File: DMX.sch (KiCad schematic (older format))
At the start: 12 parts, among them SW1 SW_DIP_x09, U10 ST485CDR, U11 NPIC6C596

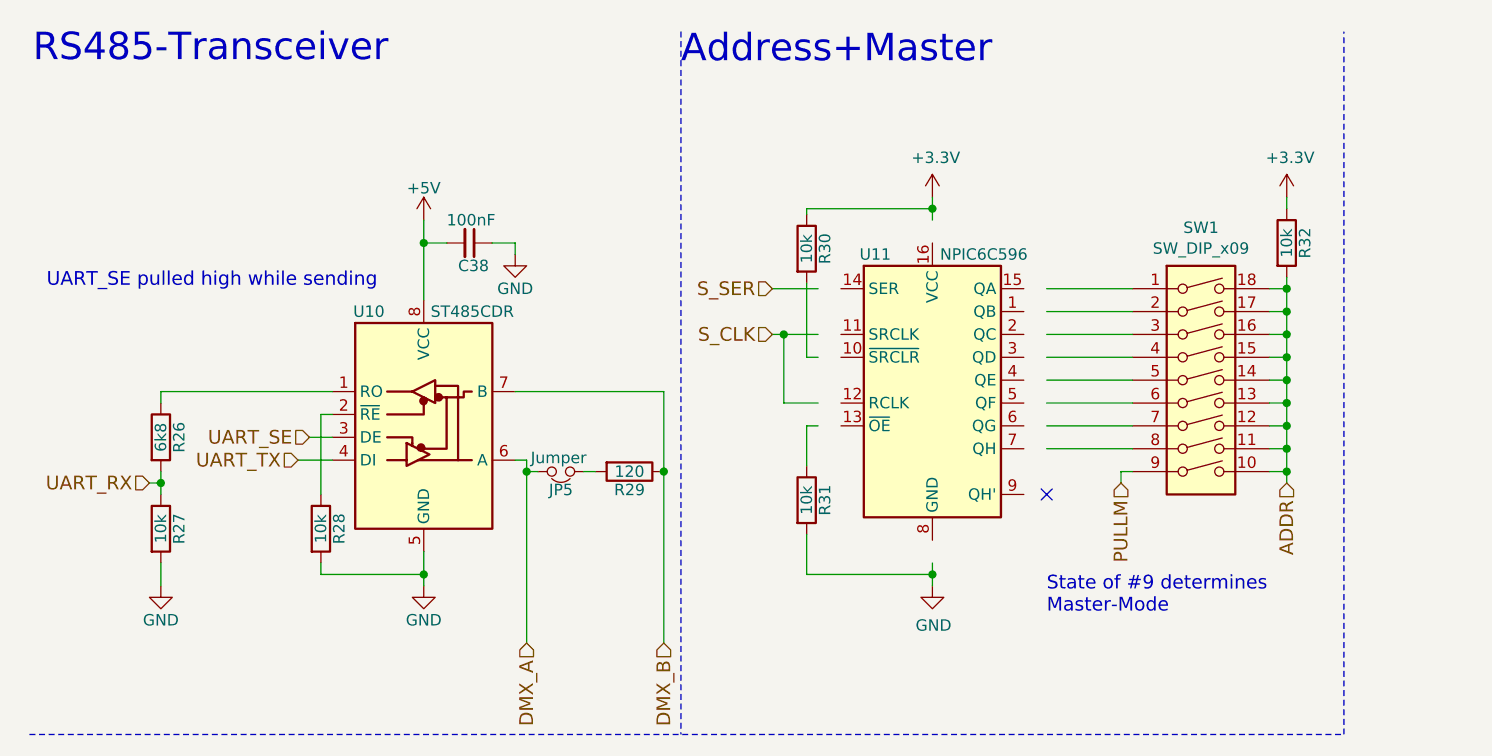
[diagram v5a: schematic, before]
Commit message: Migrated connectors to new libraries
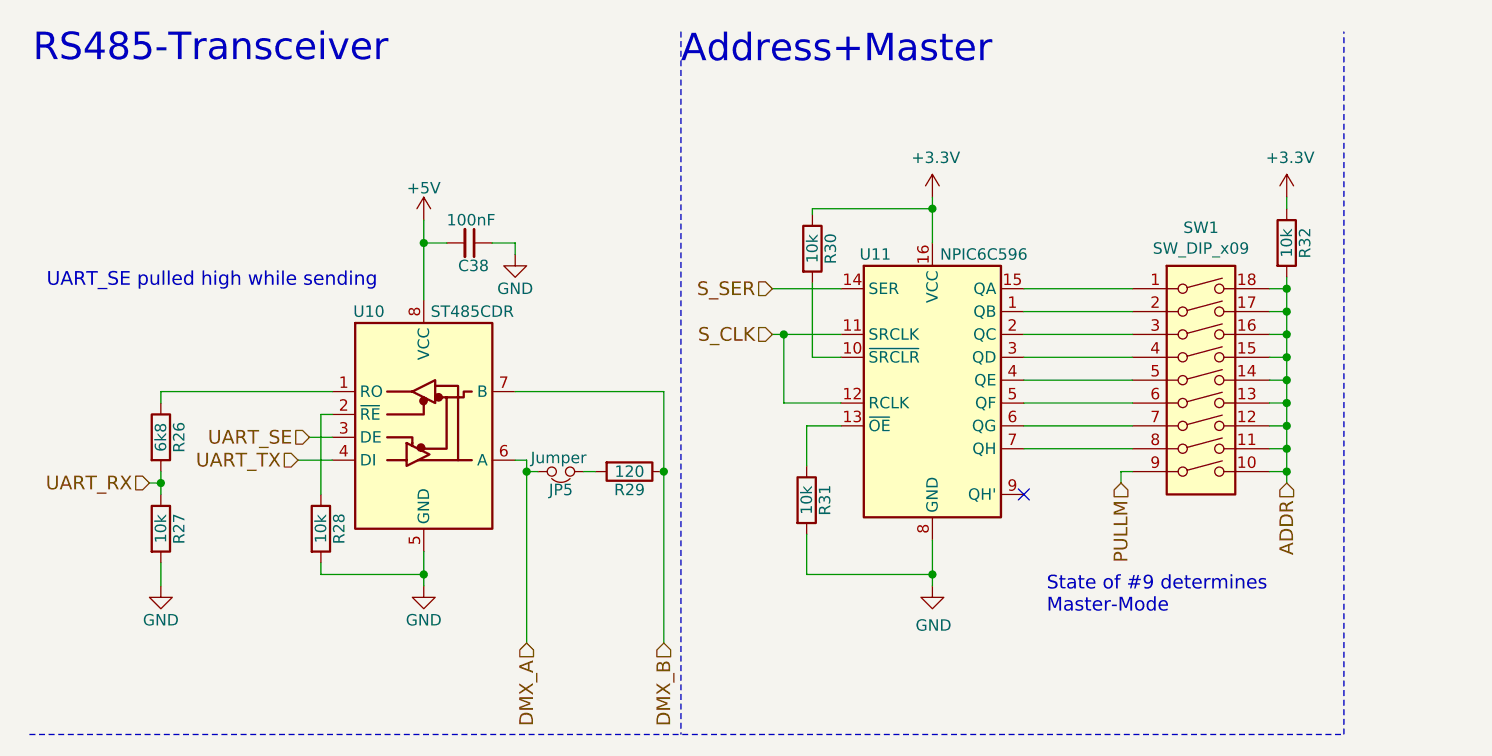
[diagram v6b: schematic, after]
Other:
- moved on the sheet: R30
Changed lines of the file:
@@
 $EndComp
 Wire Wire Line
-	4425 1250 4425 1300
+	4425 1250 4425 1400
 $Comp
 L power:GND #PWR096
@@
 $EndComp
 Wire Wire Line
-	4425 2850 4425 2800
-NoConn ~ 4925 2500
+	4425 2850 4425 2700
+NoConn ~ 4825 2500
 $Comp
 L Switch:SW_DIP_x09 SW1
@@
 $EndComp
 Wire Wire Line
-	4925 1600 5300 1600
+	4825 1600 5300 1600
 Wire Wire Line
-	4925 1800 5300 1800
+	4825 1800 5300 1800
 Wire Wire Line
-	5300 1900 4925 1900
+	5300 1900 4825 1900
 Wire Wire Line
-	4925 2000 5300 2000
+	4825 2000 5300 2000
 Wire Wire Line
-	5300 2100 4925 2100
+	5300 2100 4825 2100
 Wire Wire Line
-	4925 2200 5300 2200
+	4825 2200 5300 2200
 Wire Wire Line
-	4925 2300 5300 2300
+	4825 2300 5300 2300
 Wire Wire Line
-	4925 1700 5300 1700
+	4825 1700 5300 1700
 Wire Wire Line
 	5975 1550 5975 1600
@@
 	3875 2375 3875 2200
 Wire Wire Line
-	3875 2200 3925 2200
+	3875 2200 4025 2200
 $Comp
 L Device:R R30
 U 1 1 5B61520A
-P 3875 1425
-F 0 "R30" V 3955 1425 50  0000 C CNN
-F 1 "10k" V 3875 1425 50  0000 C CNN
-F 2 "Resistor_SMD:R_0603_1608Metric" V 3805 1425 50  0001 C CNN
-F 3 "" H 3875 1425 50  0001 C CNN
-F 4 "https://www.digikey.com/product-detail/en/bourns-inc/CR0603-FX-1002HLF/CR0603-FX-1002HLFCT-ND/3925297" V 3875 1425 50  0001 C CNN "Buy"
-	1    3875 1425
+P 3900 1425
+F 0 "R30" V 3980 1425 50  0000 C CNN
+F 1 "10k" V 3900 1425 50  0000 C CNN
+F 2 "Resistor_SMD:R_0603_1608Metric" V 3830 1425 50  0001 C CNN
+F 3 "" H 3900 1425 50  0001 C CNN
+F 4 "https://www.digikey.com/product-detail/en/bourns-inc/CR0603-FX-1002HLF/CR0603-FX-1002HLFCT-ND/3925297" V 3900 1425 50  0001 C CNN "Buy"
+	1    3900 1425
 	1    0    0    -1
 $EndComp
 Wire Wire Line
-	3875 1900 3875 1575
+	3900 1900 3900 1575
 Wire Wire Line
 	3875 2675 3875 2850
 Wire Wire Line
-	3875 1900 3925 1900
+	3900 1900 4025 1900
 Text HLabel 3725 1600 0    60   Input ~ 0
 S_SER
 Wire Wire Line
-	3725 1600 3925 1600
+	3725 1600 4025 1600
 Text HLabel 3725 1800 0    60   Input ~ 0
 S_CLK
@@
 	3775 1800 3775 2100
 Wire Wire Line
-	3775 2100 3925 2100
+	3775 2100 4025 2100
 Connection ~ 3775 1800
 Wire Wire Line
-	3775 1800 3925 1800
+	3775 1800 4025 1800
 Text HLabel 5250 2450 3    60   Input ~ 0
 PULLM
@@
 Connection ~ 4425 2850
 Wire Wire Line
-	3875 1275 3875 1250
+	3900 1275 3900 1250
 Wire Wire Line
-	3875 1250 4425 1250
+	3900 1250 4425 1250
 Connection ~ 4425 1250
 Wire Wire Line

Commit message: Replaced OOS 10k-Resistor
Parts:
- R27, R28, R30, R31, R32: Buy https://www.digikey.com/product-detail/en/bourns-inc/CR0603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 -> https://www.digikey.com/short/jw22d4
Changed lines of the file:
@@
 F 2 "Resistor_SMD:R_0603_1608Metric" V 980 2650 50  0001 C CNN
 F 3 "" H 1050 2650 50  0001 C CNN
-F 4 "https://www.digikey.com/product-detail/en/bourns-inc/CR0603-FX-1002HLF/CR0603-FX-1002HLFCT-ND/3925297" V 1050 2650 50  0001 C CNN "Buy"
+F 4 "https://www.digikey.com/short/jw22d4" V 1050 2650 50  0001 C CNN "Buy"
 	1    1050 2650
 	1    0    0    -1
@@
 F 2 "Resistor_SMD:R_0603_1608Metric" V 1680 2650 50  0001 C CNN
 F 3 "" H 1750 2650 50  0001 C CNN
-F 4 "https://www.digikey.com/product-detail/en/bourns-inc/CR0603-FX-1002HLF/CR0603-FX-1002HLFCT-ND/3925297" V 1750 2650 50  0001 C CNN "Buy"
+F 4 "https://www.digikey.com/short/jw22d4" V 1750 2650 50  0001 C CNN "Buy"
 	1    1750 2650
 	1    0    0    -1
@@
 F 2 "Resistor_SMD:R_0603_1608Metric" V 5905 1400 50  0001 C CNN
 F 3 "" H 5975 1400 50  0001 C CNN
-F 4 "https://www.digikey.com/product-detail/en/bourns-inc/CR0603-FX-1002HLF/CR0603-FX-1002HLFCT-ND/3925297" V 5975 1400 50  0001 C CNN "Buy"
+F 4 "https://www.digikey.com/short/jw22d4" V 5975 1400 50  0001 C CNN "Buy"
 	1    5975 1400
 	1    0    0    -1
@@
 F 2 "Resistor_SMD:R_0603_1608Metric" V 3805 2525 50  0001 C CNN
 F 3 "" H 3875 2525 50  0001 C CNN
-F 4 "https://www.digikey.com/product-detail/en/bourns-inc/CR0603-FX-1002HLF/CR0603-FX-1002HLFCT-ND/3925297" V 3875 2525 50  0001 C CNN "Buy"
+F 4 "https://www.digikey.com/short/jw22d4" V 3875 2525 50  0001 C CNN "Buy"
 	1    3875 2525
 	1    0    0    -1
@@
 F 2 "Resistor_SMD:R_0603_1608Metric" V 3830 1425 50  0001 C CNN
 F 3 "" H 3900 1425 50  0001 C CNN
-F 4 "https://www.digikey.com/product-detail/en/bourns-inc/CR0603-FX-1002HLF/CR0603-FX-1002HLFCT-ND/3925297" V 3900 1425 50  0001 C CNN "Buy"
+F 4 "https://www.digikey.com/short/jw22d4" V 3900 1425 50  0001 C CNN "Buy"
 	1    3900 1425
 	1    0    0    -1

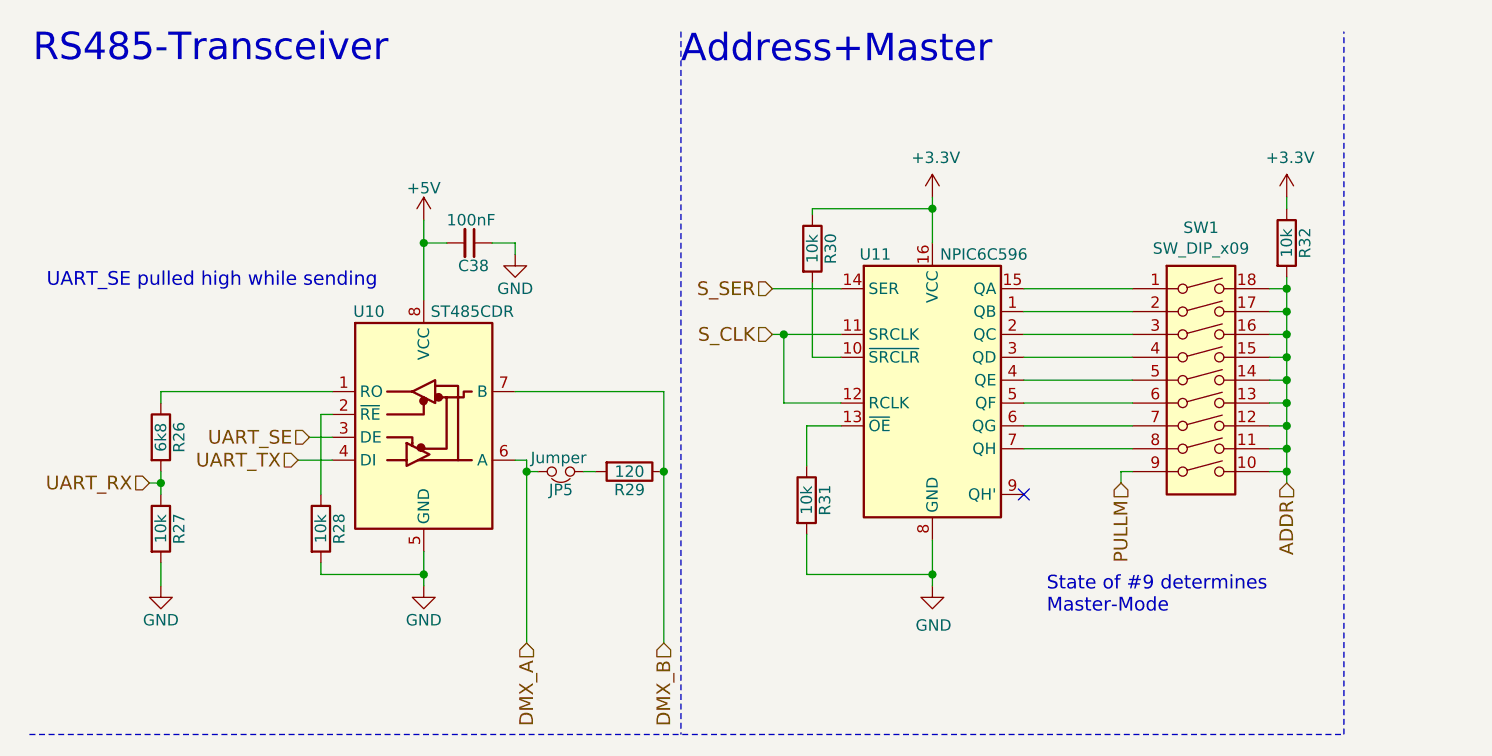
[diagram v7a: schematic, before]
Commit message: Added TestPoints to the DMX-Schematic
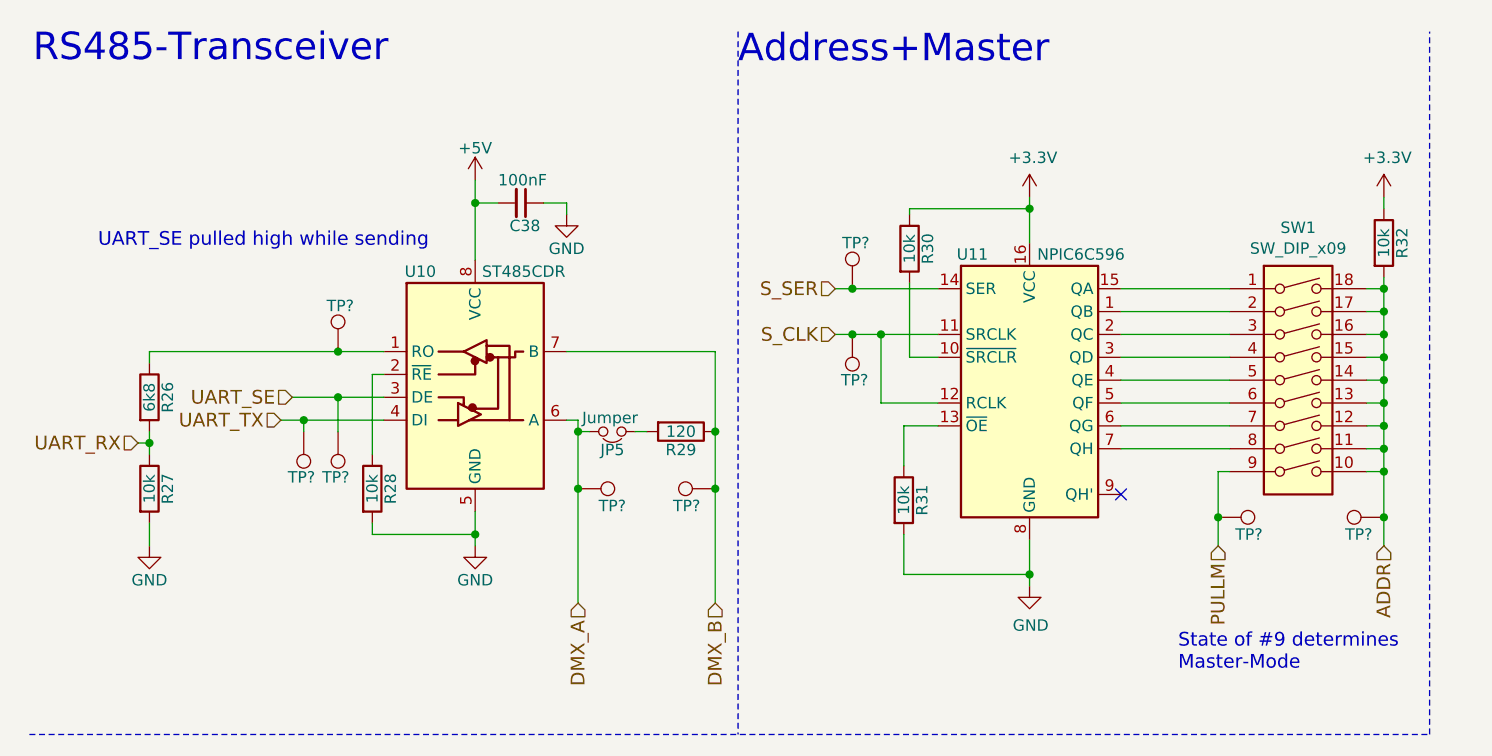
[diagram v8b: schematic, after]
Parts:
- added TP? (x9): TestPoint, symbol Connector:TestPoint
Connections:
- net ADDR: now also TP?.1
- net DMX_A: now also TP?.1
- net DMX_B: now also TP?.1
- net PULLM: now also TP?.1
- net S_CLK: now also TP?.1
- net S_SER: now also TP?.1
- net UART_SE: now also TP?.1
- net UART_TX: now also TP?.1
- net at R26.1, U10.1 (RO): now also TP?.1
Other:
- moved on the sheet: C38, JP5, R26, R27, R28, R29, R30, R31, R32, SW1, U10, U11
